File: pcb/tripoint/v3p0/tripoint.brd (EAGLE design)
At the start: 31.8 x 27.5 mm, 69 parts, among them J2 TC2030-JLINK-NL, T1 HHM1595A1, U1 STM32F091CC, U2 DW1000, U3 SKY13317, U4 LXDC2HN18A, X1 38.4M, X2 16M

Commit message: finished routing of TriPoint
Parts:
- moved C8 1.84 mm to (-3.10, -0.30), turned to 0 degrees
- moved C30 1.47 mm to (-11.3, 5.59)
- moved C43 1.31 mm to (-1.83, -0.48)
- moved R3 1.18 mm to (-11.8, 3.91)
- moved C40 0.87 mm to (3.53, 5.08), turned to 180 degrees
- moved TP3 0.78 mm to (0.69, -0.46)
- moved T1 0.74 mm to (-6.50, -1.65)
- moved C1 0.71 mm to (-6.27, -0.08)
- moved C2 0.71 mm to (-6.76, -0.08)
- moved C20 0.71 mm to (-7.29, -0.08)
- moved TP4 0.69 mm to (0.69, -1.37)
- moved C21 0.63 mm to (-3.56, -1.14)
- moved C22 0.58 mm to (-3.61, -0.30)
- moved C18 0.57 mm to (-4.14, -1.14)
- moved C19 0.53 mm to (-4.17, -0.30)
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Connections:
- net 1V8 renamed +1V8
- removed net 3V3: C16.P$1, C17.P$1, C18.P$1, C19.P$1, C20.P$1, C21.P$1, C22.P$1, C23.P$1, C24.P$1, C25.P$1, C3.2, C34.P$1, C35.P$1, C36.P$1, C37.P$1, C38.P$1, C39.P$1, C40.P$1, C41.P$1, C43.1, U2.15, U2.18, U2.19, U2.25, U2.28, U2.47, U4.1
- net +3V3: now also C16.P$1, C17.P$1, C18.P$1, C19.P$1, C20.P$1, C21.P$1, C22.P$1, C23.P$1, C24.P$1, C25.P$1, C3.2, C34.P$1, C35.P$1, C36.P$1, C37.P$1, C38.P$1, C39.P$1, C40.P$1, C41.P$1, C43.1, U2.15, U2.18, U2.19, U2.25, U2.28, U2.47, U4.1
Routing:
- net +3V3: track 0.00 -> 87.1 mm, vias 0 -> 5
- net GND: track 0.00 -> 48.4 mm, vias 0 -> 17
- net +1V8: track 0.00 -> 31.5 mm, vias 0 -> 3
- net DW_IRQ: track 0.00 -> 20.4 mm, vias 0 -> 2
- net VDDDIG: track 0.00 -> 15.5 mm, vias 0 -> 2
- net LED_RED: track 0.00 -> 14.8 mm, vias 0 -> 2
- net DW_SPI_CLK: track 0.00 -> 14.5 mm, vias 0 -> 2
- net STM_SWDIO: track 0.00 -> 14.0 mm, vias 0 -> 2
- net REG_EN: track 0.00 -> 13.8 mm, vias 0 -> 2
- net LED_BLUE: track 0.00 -> 13.5 mm, vias 0 -> 2
- net LED_GREEN: track 0.00 -> 12.2 mm, vias 0 -> 2
- net DW_SPI_MISO: track 0.00 -> 11.7 mm, vias 0 -> 2
- net DW_SPI_MOSI: track 0.00 -> 11.2 mm, vias 0 -> 2
- net STM_SWCLK: track 0.00 -> 10.5 mm, vias 0 -> 2
- net !STM_RST: track 0.00 -> 9.54 mm, vias 0 -> 2
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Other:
- board text added: "13/07/2018"
- board text removed: "12/07/2018"

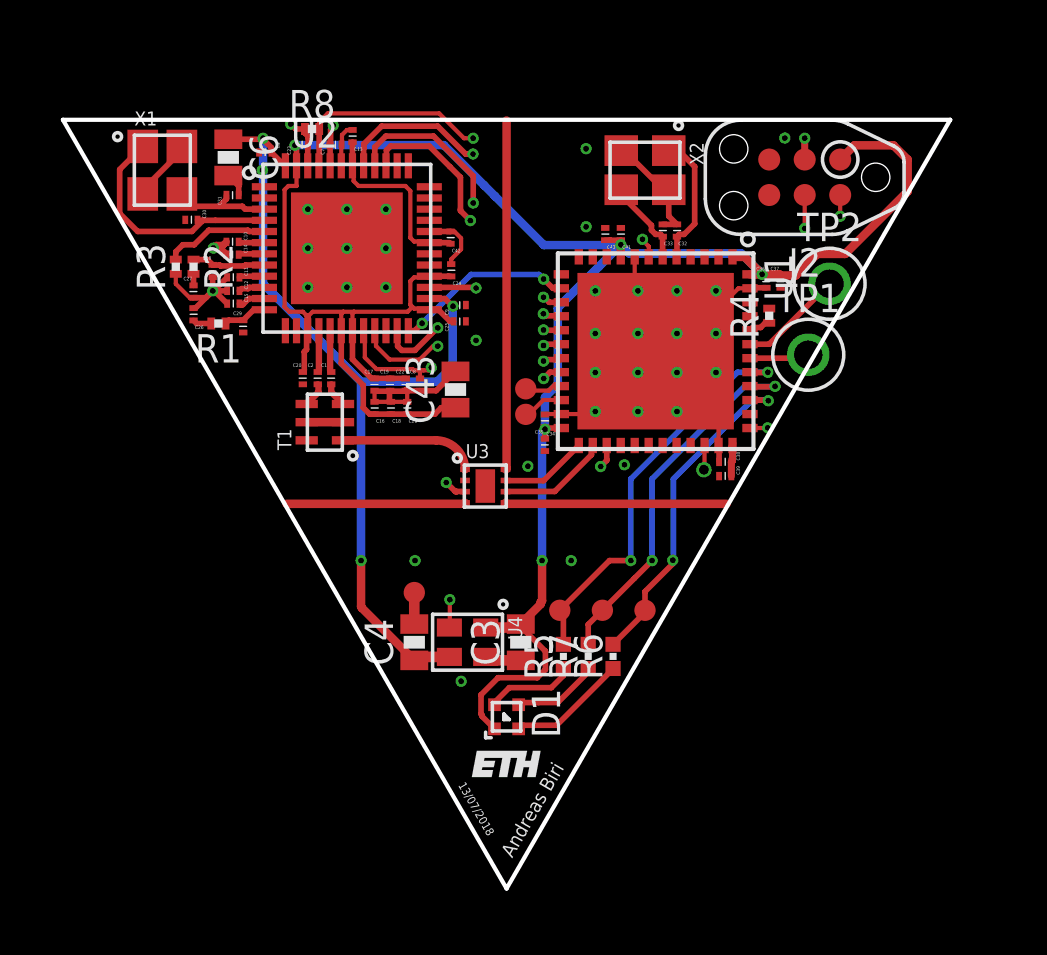
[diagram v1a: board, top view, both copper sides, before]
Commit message: buried power plane, increased distance between SPI and RF traces
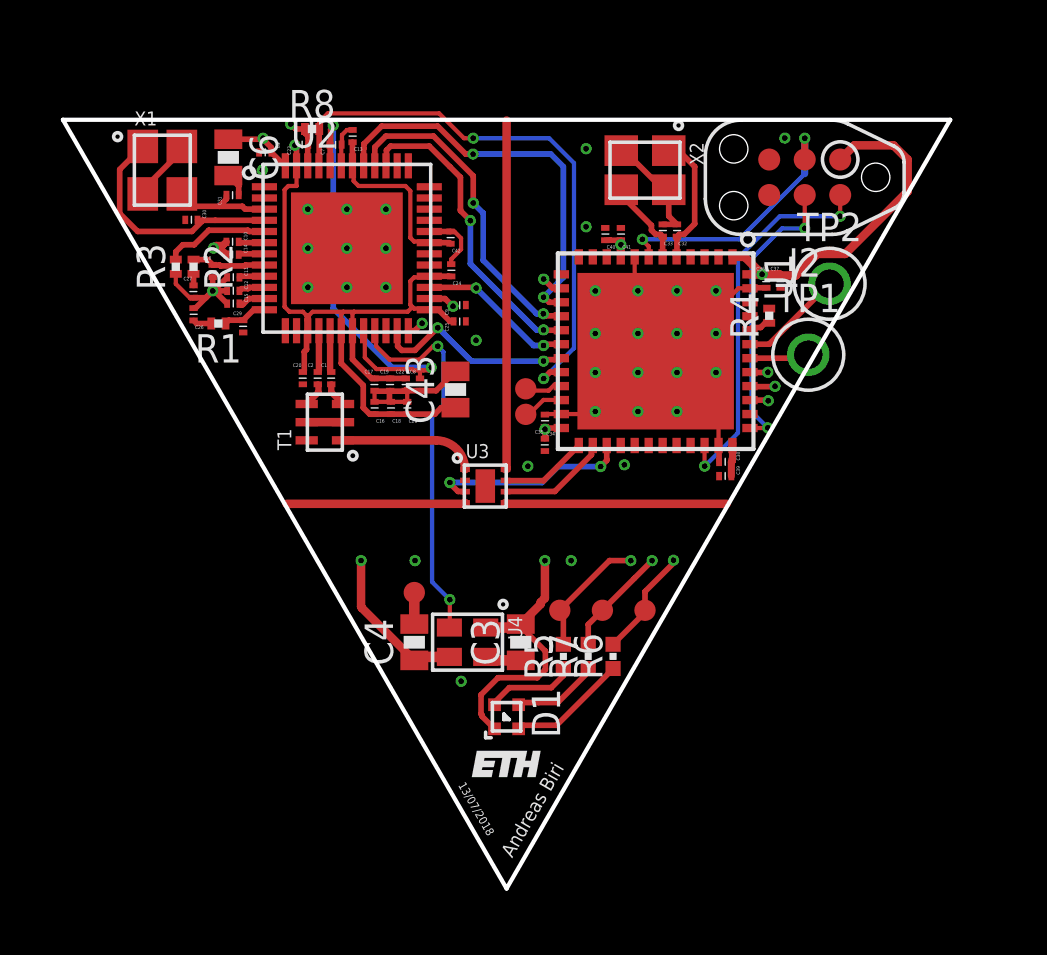
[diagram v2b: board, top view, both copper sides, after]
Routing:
- net VDDDIG: track 15.5 -> 16.3 mm

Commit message: added second pass of TriPoint schematic and component positions
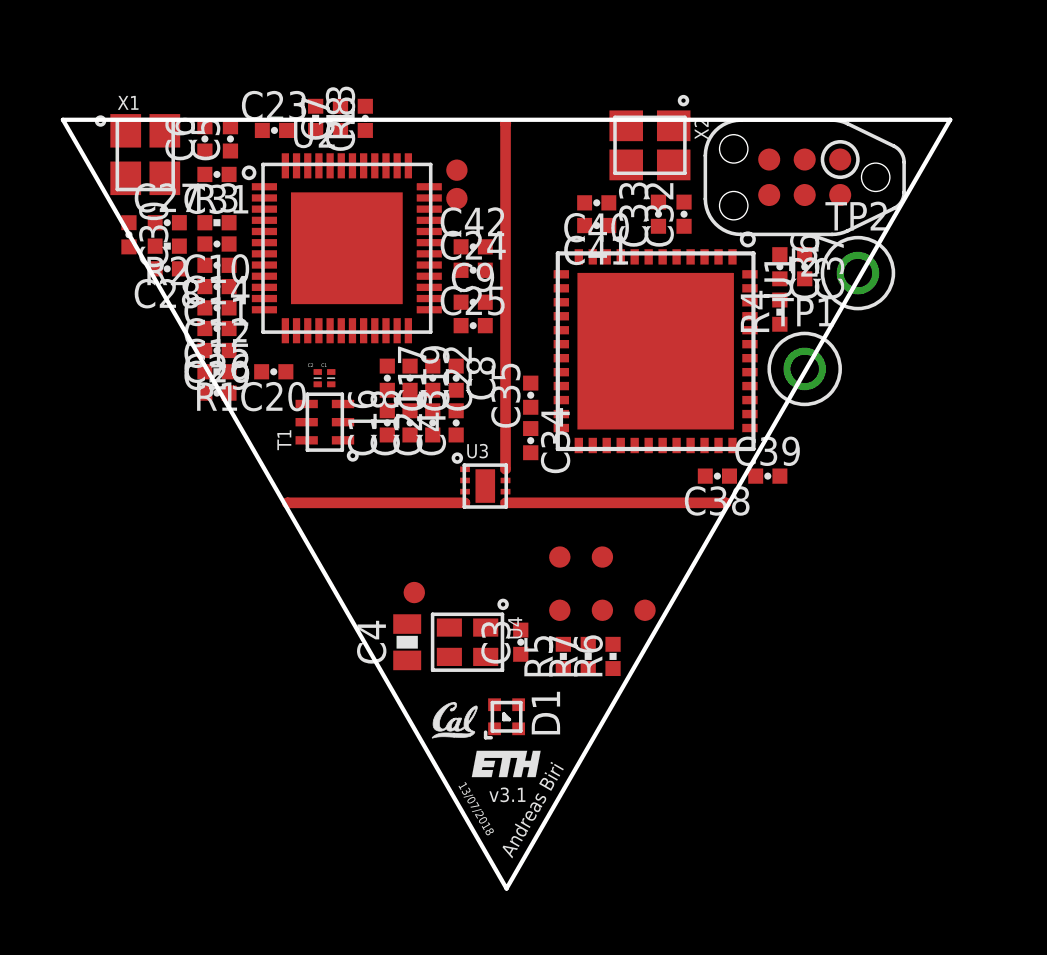
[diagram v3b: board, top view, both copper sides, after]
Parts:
- added TP10, TP9: TEST-POINT, headers:PAD.03X.03
- added U$2: (no value), logos:UCB_CAL_50MIL
- C10, C11, C12, C13, C14, C15, C16, C17, C18, C19, C20, C21, C22, C23, C24, C25, C26, C27, C28, C29, C30, C31, C32, C33, C34, C35, C36, C37, C38, C39, C40, C41, C42, C5, C7, C8, C9: device passives:0201_CAP -> passives:0402_CAP
- C3, C43, C6: device passives:0603_CAP -> passives:0402_CAP
- R1, R2, R3, R4, R8: device passives:0201_RES -> passives:0402_RES
- moved TP3 6.62 mm to (3.43, -6.48)
- moved TP4 5.25 mm to (1.91, -6.48)
- moved C26 2.94 mm to (-10.4, -0.61), turned to 0 degrees
- moved C27 2.64 mm to (-12.1, 5.49)
- moved C30 2.30 mm to (-13.5, 5.05)
- moved R3 2.16 mm to (-10.4, 5.49), turned to 0 degrees
- moved C35 1.85 mm to (0.86, -0.69), turned to 90 degrees
- moved R1 1.73 mm to (-10.4, 0.15)
- moved C28 1.63 mm to (-12.1, 3.84), turned to 180 degrees
- moved C39 1.52 mm to (9.35, -3.58), turned to 0 degrees
- moved C5 1.33 mm to (-9.88, 8.48), turned to 90 degrees
- moved C8 1.32 mm to (-1.80, -0.08), turned to 270 degrees
- moved C29 1.28 mm to (-10.4, 0.91), turned to 180 degrees
- moved R2 1.19 mm to (-12.1, 4.65), turned to 180 degrees
- moved C43 1.19 mm to (-1.80, -1.68)
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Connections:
- new net N$13: TP9.P$1, U2.36
- new net N$14: TP10.P$1, U2.35
- net +1V8: now also C5.1, C9.1; no longer C5.P$1, C9.P$1
- net +3V3: now also C16.1, C17.1, C18.1, C19.1, C20.1, C21.1, C22.1, C23.1, C24.1, C25.1, C34.1, C35.1, C36.1, C37.1, C38.1, C39.1, C40.1, C41.1; no longer C16.P$1, C17.P$1, C18.P$1, C19.P$1, C20.P$1, C21.P$1, C22.P$1, C23.P$1, C24.P$1, C25.P$1, C34.P$1, C35.P$1, C36.P$1, C37.P$1, C38.P$1, C39.P$1, C40.P$1, C41.P$1
- net GND: now also C10.2, C11.2, C12.2, C13.2, C14.2, C15.2, C16.2, C17.2, C18.2, C19.2, C20.2, C21.2, C22.2, C23.2, C24.2, C25.2, C26.2, C27.2, C28.2, C29.2, C30.2, C31.2, C32.2, C33.2, C34.2, C35.2, C36.2, C37.2, C38.2, C39.2, C40.2, C41.2, C42.2, C5.2, C7.2, C8.2, C9.2; no longer C10.P$2, C11.P$2, C12.P$2, C13.P$2, C14.P$2, C15.P$2, C16.P$2, C17.P$2, C18.P$2, C19.P$2, C20.P$2, C21.P$2, C22.P$2, C23.P$2, C24.P$2, C25.P$2, C26.P$2, C27.P$2, C28.P$2, C29.P$2, C30.P$2, C31.P$2, C32.P$2, C33.P$2, C34.P$2, C35.P$2, C36.P$2, C37.P$2, C38.P$2, C39.P$2, C40.P$2, C41.P$2, C42.P$2, C5.P$2, C7.P$2, C8.P$2, C9.P$2
- net GPIO2: now also U1.29; no longer U1.21
- net GPIO3: now also U1.28; no longer U1.22
- net LED_BLUE: now also TP7.P$1; no longer TP6.P$1
- net LED_GREEN: now also TP6.P$1; no longer TP5.P$1
- net LED_RED: now also TP5.P$1; no longer TP7.P$1
- net N$4: now also C26.1; no longer C26.P$1
- net N$5: now also C27.1; no longer C27.P$1
- net N$6: now also C29.1; no longer C29.P$1
- net N$9: now also C28.1; no longer C28.P$1
- net OSC_IN: now also C32.1; no longer C32.P$1
- net OSC_OUT: now also C33.1; no longer C33.P$1
- net VDDCLK: now also C11.1; no longer C11.P$1
- net VDDDIG: now also C7.1, C8.1; no longer C7.P$1, C8.P$1
- net VDDIF: now also C14.1; no longer C14.P$1
- net VDDIO: now also C13.1, C42.1; no longer C13.P$1, C42.P$1
- net VDDMS: now also C10.1; no longer C10.P$1
- net VDDSYN: now also C12.1; no longer C12.P$1
- net VDDVCO: now also C15.1; no longer C15.P$1
- net XTAL1: now also C31.1; no longer C31.P$1
- net XTAL2: now also C30.1; no longer C30.P$1
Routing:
- net +3V3: track 87.1 -> 0.00 mm, vias 5 -> 0
- net GND: track 48.4 -> 0.00 mm, vias 17 -> 0
- net +1V8: track 31.5 -> 0.00 mm, vias 3 -> 0
- net DW_IRQ: track 20.4 -> 0.00 mm, vias 2 -> 0
- net VDDDIG: track 16.3 -> 0.00 mm, vias 2 -> 0
- net LED_RED: track 14.8 -> 0.00 mm, vias 2 -> 0
- net DW_SPI_CLK: track 14.5 -> 0.00 mm, vias 2 -> 0
- net REG_EN: track 13.8 -> 0.00 mm, vias 2 -> 0
- net STM_SWDIO: track 13.7 -> 0.00 mm, vias 2 -> 0
- net LED_BLUE: track 13.5 -> 0.00 mm, vias 2 -> 0
- net LED_GREEN: track 12.2 -> 0.00 mm, vias 2 -> 0
- net DW_SPI_MISO: track 11.7 -> 0.00 mm, vias 2 -> 0
- net DW_SPI_MOSI: track 11.2 -> 0.00 mm, vias 2 -> 0
- net STM_SWCLK: track 10.5 -> 0.00 mm, vias 2 -> 0
- net !STM_RST: track 9.54 -> 0.00 mm, vias 2 -> 0
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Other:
- board text added: "v3.1"

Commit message: switched from triangle to square :-/
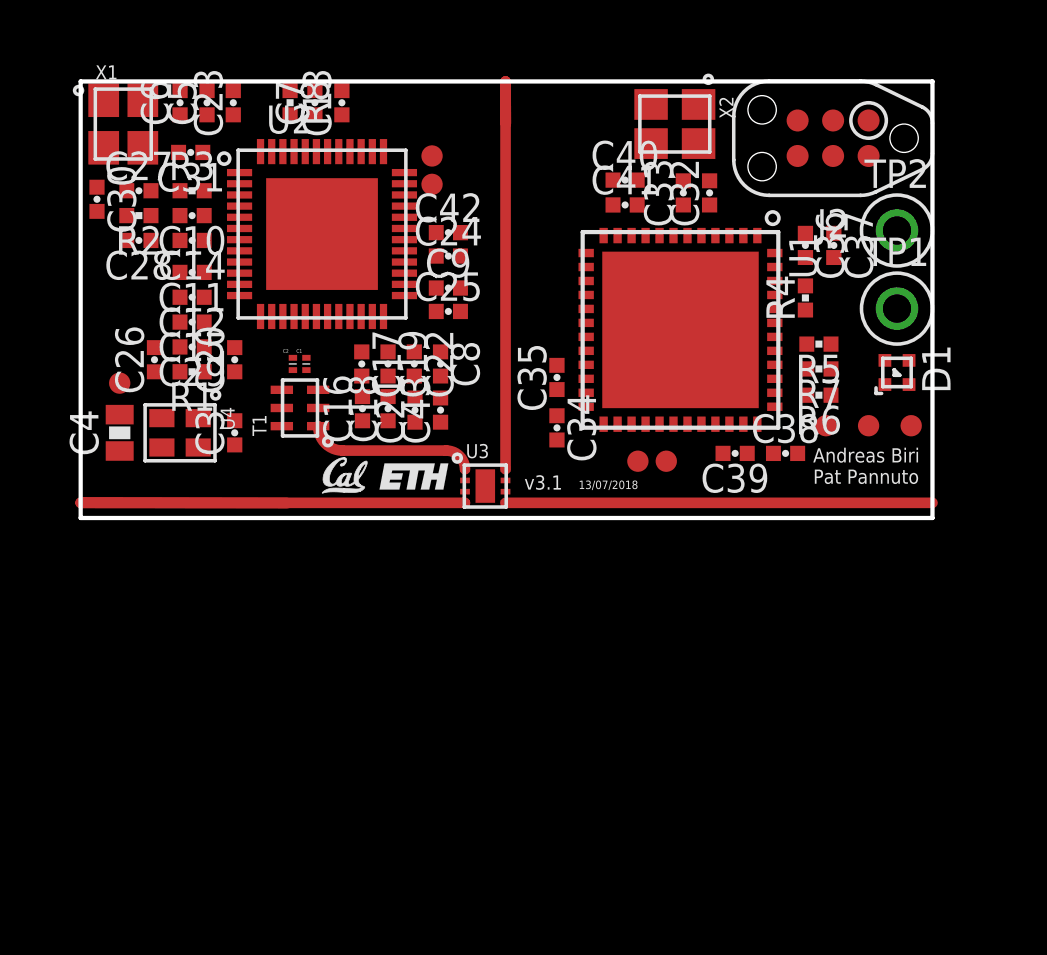
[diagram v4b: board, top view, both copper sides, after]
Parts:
- moved D1 18.6 mm to (14.0, 0.13)
- moved R5 14.4 mm to (11.2, 1.14), turned to 180 degrees
- moved R7 13.2 mm to (11.2, 0.25), turned to 180 degrees
- moved TP8 12.9 mm to (-13.8, -0.25)
- moved TP7 12.9 mm to (13.0, -1.78)
- moved C4 12.7 mm to (-13.8, -2.03)
- moved U4 12.7 mm to (-11.7, -2.03)
- moved C3 12.7 mm to (-9.73, -2.03)
- moved R6 11.9 mm to (11.2, -0.69), turned to 180 degrees
- moved TP5 11.6 mm to (14.5, -1.78)
- moved U$1 10.8 mm to (-3.43, -4.06)
- moved TP6 10.4 mm to (11.4, -1.78)
- moved U$2 9.61 mm to (-6.60, -4.19)
- moved TP4 4.42 mm to (4.70, -3.05)
- moved TP3 4.12 mm to (5.71, -3.05)
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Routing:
- net RF1: track 6.37 -> 21.1 mm
- net RF2: track 7.89 -> 15.3 mm
- net N$1: track 0.00 -> 5.89 mm
- net RF3: track 12.4 -> 15.4 mm
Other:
- board size 31.8 x 27.5 mm -> 30.5 x 15.6 mm
- board text added: "Andreas Biri Pat Pannuto"
- board text removed: "Andreas Biri"

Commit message: finished second pass of TriPoint
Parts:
- C38: value 100nF -> 4.7uF
- C39: value 4.7uF -> 100nF
- C40: value 10nF -> 1uF
- C41: value 1uF -> 10nF
- moved C27 4.71 mm to (-13.4, 1.93)
- moved TP6 3.09 mm to (14.5, -2.29)
- moved R3 3.00 mm to (-13.9, 5.26), turned to 90 degrees
- moved R2 2.93 mm to (-13.4, 2.82)
- moved TP5 2.84 mm to (11.7, -2.29)
- moved R5 2.07 mm to (11.4, -0.91)
- moved C10 1.79 mm to (-13.0, 5.26), turned to 270 degrees
- moved R6 1.66 mm to (11.4, 0.97)
- moved C28 1.17 mm to (-13.4, 3.71)
- moved C30 1.06 mm to (-14.9, 5.28)
- moved C19 0.94 mm to (-3.30, 0.46)
- moved C22 0.91 mm to (-2.39, 0.46)
- moved C8 0.86 mm to (-1.50, 0.46)
- moved TP8 0.85 mm to (-14.2, 0.51)
- moved TP9 0.74 mm to (-2.03, 8.26)
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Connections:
- net LED_BLUE: no longer TP7.P$1
- net LED_GREEN: now also U1.41; no longer TP6.P$1, U1.39
- net LED_RED: now also U1.39; no longer TP5.P$1, U1.41
- net N$10: now also TP5.P$1
- net N$11: now also TP7.P$1
- net N$12: now also TP6.P$1
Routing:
- net +3V3: track 0.00 -> 118.1 mm, vias 0 -> 10
- net GND: track 0.00 -> 83.8 mm, vias 0 -> 135
- net +1V8: track 0.00 -> 31.1 mm, vias 0 -> 3
- net DW_IRQ: track 0.00 -> 21.7 mm, vias 0 -> 2
- net VDDDIG: track 0.00 -> 17.7 mm, vias 0 -> 2
- net STM_SWDIO: track 0.00 -> 14.8 mm, vias 0 -> 2
- net DW_SPI_CLK: track 0.00 -> 13.4 mm, vias 0 -> 2
- net DW_SPI_MISO: track 0.00 -> 12.7 mm, vias 0 -> 2
- net DW_SPI_MOSI: track 0.00 -> 11.9 mm, vias 0 -> 2
- net STM_SWCLK: track 0.00 -> 10.2 mm, vias 0 -> 2
- net XTAL2: track 0.00 -> 9.42 mm, vias 0 -> 2
- net !STM_RST: track 0.00 -> 9.31 mm, vias 0 -> 2
- net REG_EN: track 0.00 -> 9.14 mm, vias 0 -> 2
- net DW_WAKEUP: track 0.00 -> 8.86 mm, vias 0 -> 2
- net ANT_SEL1: track 0.00 -> 8.64 mm, vias 0 -> 2
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- added copper zone on layer 1, net N$1
- added copper zone on layer 1, net N$15
- added copper zone on layer 1, net RF3
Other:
- board text added: "Andreas Biri, Pat Pannuto"
- board text removed: "Andreas Biri Pat Pannuto"

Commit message: finished third pass, SquarePoint it is
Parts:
- R3: value 11k -> 11k 1%
- moved U$2 10.3 mm to (-0.76, 4.32)
- moved U$1 5.11 mm to (1.65, -4.57)
- moved C33 3.51 mm to (3.38, 8.48), turned to 180 degrees
- moved C32 3.00 mm to (6.91, 9.55), turned to 180 degrees
- moved X2 1.53 mm to (6.15, 7.49)
- moved C40 0.97 mm to (3.38, 7.44), turned to 180 degrees
- moved X1 0.93 mm to (-13.0, 8.38), turned to 90 degrees
- moved C41 0.90 mm to (3.38, 6.38), turned to 180 degrees
- moved C6 0.81 mm to (-12.3, 10.3), turned to 180 degrees
- moved C31 0.51 mm to (-10.8, 7.82), turned to 270 degrees
- moved C28 0.28 mm to (-13.7, 3.71)
- moved C27 0.26 mm to (-13.7, 1.91)
- moved R2 0.25 mm to (-13.7, 2.82)
- moved C26 0.23 mm to (-13.2, 0.58)
- moved C17 0.13 mm to (-4.67, 0.05)
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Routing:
- net +3V3: track 118.1 -> 109.0 mm, vias 10 -> 13
- net XTAL2: track 9.42 -> 7.56 mm, vias 2 -> 0
- net +1V8: track 31.1 -> 32.1 mm
- net XTAL1: track 5.39 -> 4.50 mm
- net OSC_OUT: track 4.19 -> 4.77 mm
- net VDDDIG: track 17.7 -> 18.2 mm
- net GND: track 83.8 -> 84.2 mm, vias 135 -> 204
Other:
- board size 30.5 x 15.6 mm -> 30.5 x 16.4 mm
- board text added: "17/07/2018"
- board text added: "SquarePoint"
- board text removed: "13/07/2018"

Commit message: added correct RF traces and board thickness
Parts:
- moved C33 0.35 mm to (3.28, 8.15)
- moved C40 0.35 mm to (3.28, 7.11)
- moved C41 0.35 mm to (3.28, 6.05)
- moved C32 0.11 mm to (6.81, 9.60)
- moved X2 0.11 mm to (6.05, 7.54)

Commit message: finished silk for SquarePoint
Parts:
- moved U$2 1.05 mm to (0.25, 4.06)
- renumbered TP1 to GPIO0, TP2 to GPIO1
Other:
- board text added: "B"
- board text added: "G"
- board text added: "GND"
- board text added: "IO2"
- board text added: "IO3"
- board text added: "R"
